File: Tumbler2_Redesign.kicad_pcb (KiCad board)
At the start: 2 copper layers, 77 x 84 mm, 113 parts, among them J1 Conn_01x02, J2 Conn_01x05, J3 Conn_01x10, J4 Conn_01x10, J5 USB_C_Receptacle_USB2.0_16P, J6 USB_C_Receptacle_USB2.0_16P, J7 Conn_01x04, J8 Conn_01x06, J9 Conn_01x06, Q1 MMBT3904, Q3 MMBT3904, SW1 SW_Push, SW2 SW_Push, SW3 SW_Push, U1 CH340C, U11 TB6612FNG, U12 AMS1117-5.0, U2 LSM6DSV, U3 AP63203WU, U4 ESP32-S3-WROOM-1, U8 USBLC6-2SC6, U9 USBLC6-2SC6

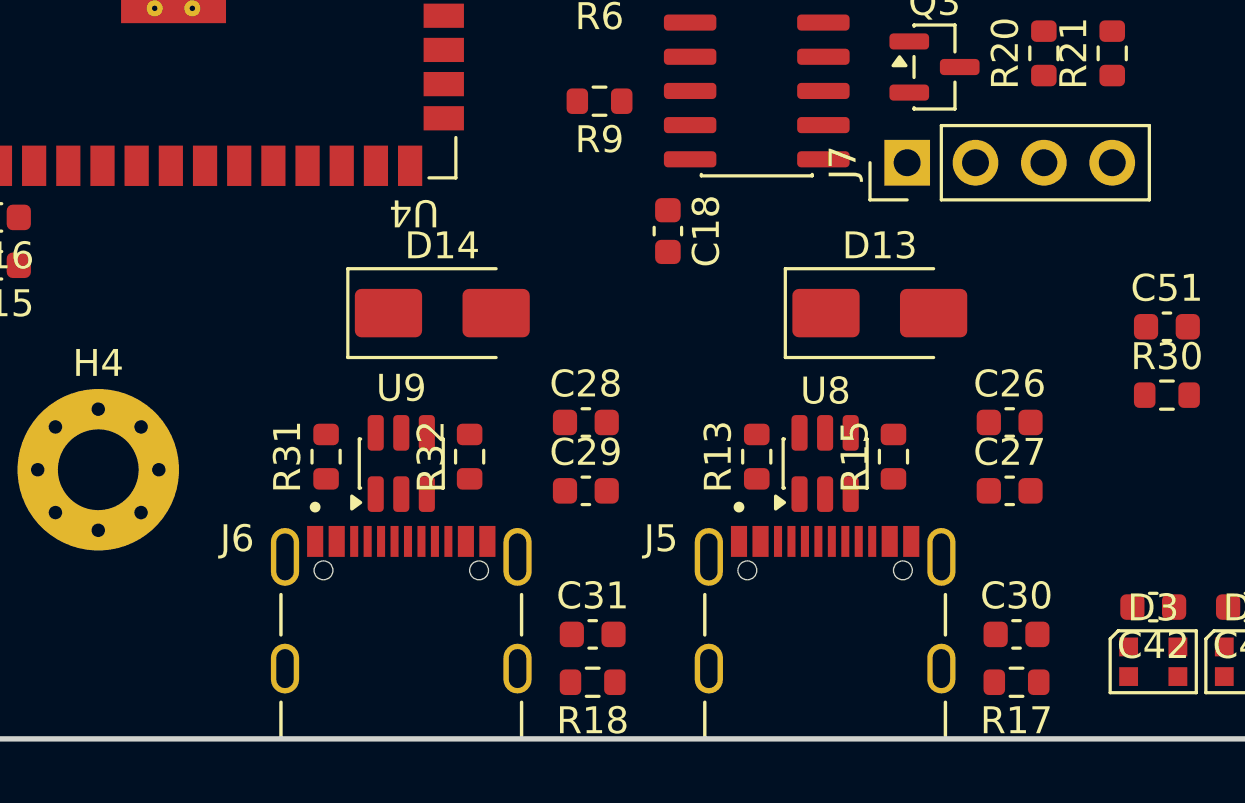
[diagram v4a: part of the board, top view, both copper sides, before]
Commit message: Fix bus merging and add net classes
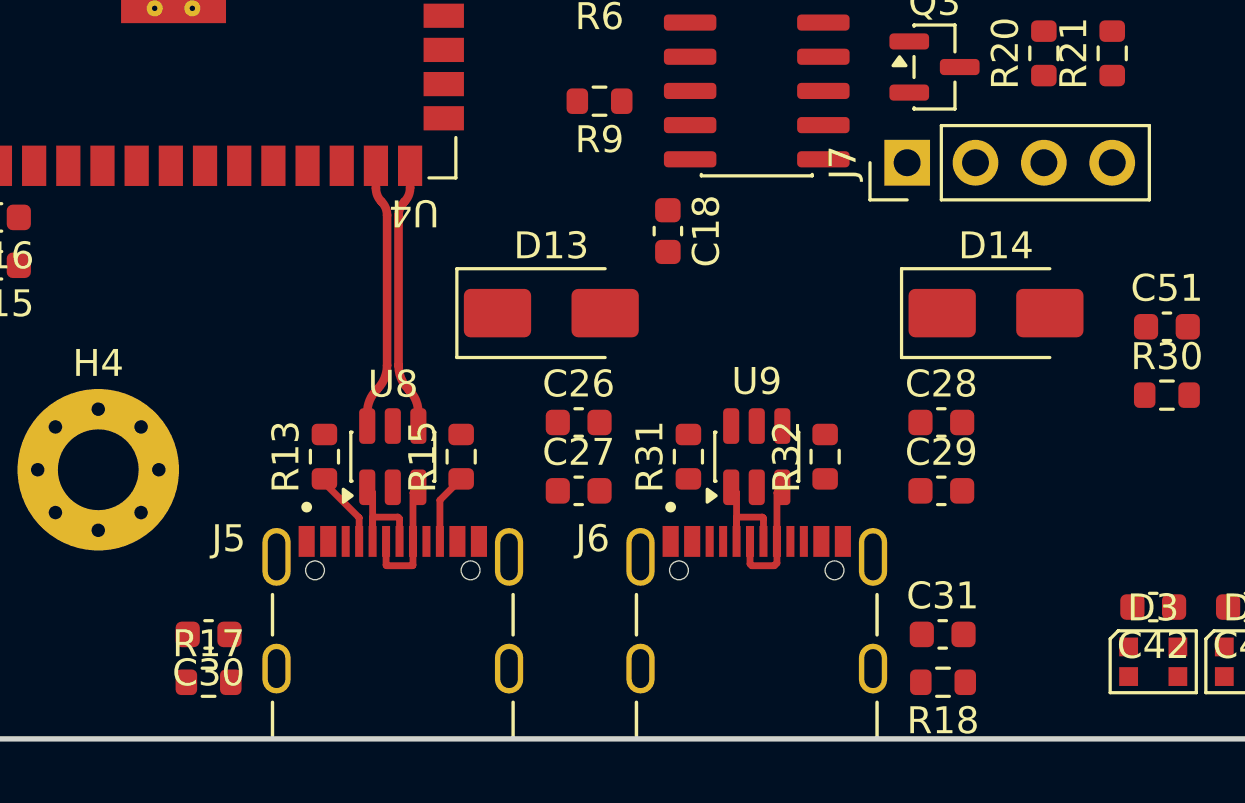
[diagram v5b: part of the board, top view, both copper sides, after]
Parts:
- moved C30 30.0 mm to (123.9, 141.5), turned to 180 degrees
- moved R17 30.0 mm to (123.9, 143.3), turned to 0 degrees
- moved D14 20.6 mm to (153.2, 129.5)
- moved U8 16.1 mm to (130.7, 134.9)
- moved J5 16.1 mm to (130.7, 142.7)
- moved R15 16.1 mm to (133.3, 134.9)
- moved R13 16.1 mm to (128.2, 134.9)
- moved C26 16.0 mm to (137.7, 133.6)
- moved C27 16.0 mm to (137.7, 136.1)
- moved R31 13.5 mm to (141.7, 134.9)
- moved U9 13.2 mm to (144.3, 134.9)
- moved C28 13.2 mm to (151.1, 133.6)
- moved C29 13.2 mm to (151.1, 136.1)
- moved J6 13.2 mm to (144.3, 142.7)
- moved R32 13.2 mm to (146.8, 134.9)
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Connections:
- J2 pad 1: /MCU/ENCA -> /MCU/ENCA_A
- J2 pad 2: /MCU/ENCB -> /MCU/ENCB_A
- J2 pad 3: /MCU/ENCA -> /MCU/ENCA_B
- J2 pad 4: /MCU/ENCB -> /MCU/ENCB_B
- R22 pad 2: /MCU/ENCB -> /MCU/ENCB_A
- R23 pad 2: /MCU/ENCA -> /MCU/ENCA_A
- R24 pad 2: /MCU/ENCB -> /MCU/ENCB_A
- R25 pad 2: /MCU/ENCA -> /MCU/ENCA_A
- R26 pad 2: /MCU/ENCB -> /MCU/ENCB_B
- R27 pad 2: /MCU/ENCA -> /MCU/ENCA_B
- R28 pad 2: /MCU/ENCB -> /MCU/ENCB_B
- R29 pad 2: /MCU/ENCA -> /MCU/ENCA_B
- U1 pad 5: /MCU/DP -> /MCU/DP_2
- U1 pad 6: /MCU/DM -> /MCU/DN_2
- U11 pad 15: /MCU/PWM -> /MCU/PWMB
- U11 pad 16: /MCU/IN2 -> /MCU/BIN2
- U11 pad 17: /MCU/IN1 -> /MCU/BIN1
- U11 pad 21: /MCU/IN1 -> /MCU/AIN1
- U11 pad 22: /MCU/IN2 -> /MCU/AIN2
- U11 pad 23: /MCU/PWM -> /MCU/PWMA
- U4 pad 10: /MCU/IN2 -> /MCU/BIN2
- U4 pad 11: /MCU/PWM -> /MCU/PWMB
- U4 pad 13: /MCU/DM -> /MCU/DN_1
- U4 pad 14: /MCU/DP -> /MCU/DP_1
- U4 pad 24: /MCU/ENCA -> /MCU/ENCA_B
- U4 pad 25: /MCU/ENCB -> /MCU/ENCB_B
- U4 pad 31: /MCU/ENCA -> /MCU/ENCA_A
- U4 pad 32: /MCU/IN1 -> /MCU/AIN1
- U4 pad 33: /MCU/IN2 -> /MCU/AIN2
- U4 pad 34: /MCU/PWM -> /MCU/PWMA
- U4 pad 35: /MCU/ENCB -> /MCU/ENCB_A
- U4 pad 9: /MCU/IN1 -> /MCU/BIN1
- U8 pad 4: /MCU/DP -> /MCU/DP_1
- U8 pad 6: /MCU/DM -> /MCU/DN_1
- U9 pad 4: /MCU/DP -> /MCU/DP_2
- U9 pad 6: /MCU/DM -> /MCU/DN_2
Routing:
- net /MCU/DP_1: track 0.00 -> 9.97 mm
- net /MCU/DN_1: track 0.00 -> 9.96 mm
- net Net-(J5-D+-PadA6): track 0.00 -> 4.87 mm
- net Net-(J6-D--PadA7): track 0.00 -> 4.86 mm
- net Net-(J5-D--PadA7): track 0.00 -> 4.85 mm
- net Net-(J6-D+-PadA6): track 0.00 -> 4.80 mm
- net Net-(J5-CC1): track 0.00 -> 2.86 mm
- net Net-(J5-CC2): track 0.00 -> 2.65 mm

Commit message: Start conceptual layouting
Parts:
- removed TP5, TP6, TP7: TestPoint, TestPoint:TestPoint_Pad_D1.5mm
- TP1, TP10, TP11, TP12, TP2, TP4: footprint TestPoint:TestPoint_Pad_D1.5mm -> TestPoint:TestPoint_THTPad_D1.0mm_Drill0.5mm
- moved R7 72.7 mm to (207.5, 106.9)
- moved R8 72.7 mm to (207.5, 103.4)
- moved TP11 51.1 mm to (207.8, 117.3)
- moved TP12 51.1 mm to (205.2, 117.3)
- moved R20 50.8 mm to (205.7, 122.1)
- moved R21 50.8 mm to (208.3, 122.1)
- moved R12 40.7 mm to (116.1, 130.6), turned to 0 degrees
- moved R11 40.0 mm to (116.1, 128.8), turned to 0 degrees
- moved C21 35.9 mm to (119.6, 127.0), turned to 0 degrees
- moved SW3 32.5 mm to (124.5, 130.8), turned to 180 degrees
- moved SW2 27.9 mm to (124.5, 125.7), turned to 180 degrees
- moved C41 26.7 mm to (139.4, 86.9), turned to 180 degrees
- moved R1 22.4 mm to (158.4, 105.4), turned to 0 degrees
- moved C32 20.5 mm to (167.6, 114.3), turned to -90 degrees
- moved TP4 19.9 mm to (145.0, 108.7)
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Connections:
- net /Peripherals/M1_M renamed /Peripherals/M1_N
- net /Peripherals/M2_M renamed /Peripherals/M2_N
- U4 pad 12: /MCU/IO8 -> /MCU/RGB
- U4 pad 23: /MCU/RGB -> /MCU/IO8
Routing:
- net /MCU/TXD: track 0.00 -> 42.9 mm
- net /MCU/RXD: track 0.00 -> 42.2 mm, vias 0 -> 2
- net /MCU/RGB: track 0.00 -> 39.4 mm, vias 0 -> 2
- net /MCU/RTS: track 0.00 -> 21.9 mm
- net /MCU/DTR: track 0.00 -> 18.5 mm, vias 0 -> 2
- net /MCU/BTN: track 0.00 -> 15.8 mm
- net /MCU/DP_2: track 0.00 -> 13.7 mm, vias 0 -> 2
- net /MCU/DN_2: track 0.00 -> 13.7 mm, vias 0 -> 2
- net /MCU/ENABLE: track 0.00 -> 12.0 mm
- net 3.3V: track 0.00 -> 9.83 mm
- net /MCU/GPIO0: track 0.00 -> 5.59 mm
- net Net-(J8-Pin_4): track 0.00 -> 3.81 mm
- net Net-(J8-Pin_3): track 0.00 -> 3.81 mm
- net Net-(J9-Pin_4): track 0.00 -> 3.80 mm
- net Net-(J9-Pin_3): track 0.00 -> 3.80 mm
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- added copper zone on F.Cu, net 3.3V
- added copper zone on B.Cu, net GND
- added copper zone on F.Cu, net GND
- added copper zone on F.Cu, net Net-(D11-A)
- added copper zone on F.Cu, net Net-(J1-Pin_2)
- added copper zone on F.Cu, net Net-(J5-SHIELD)
- added copper zone on F.Cu, net Net-(J6-SHIELD)
- added copper zone on F.Cu, net VBAT

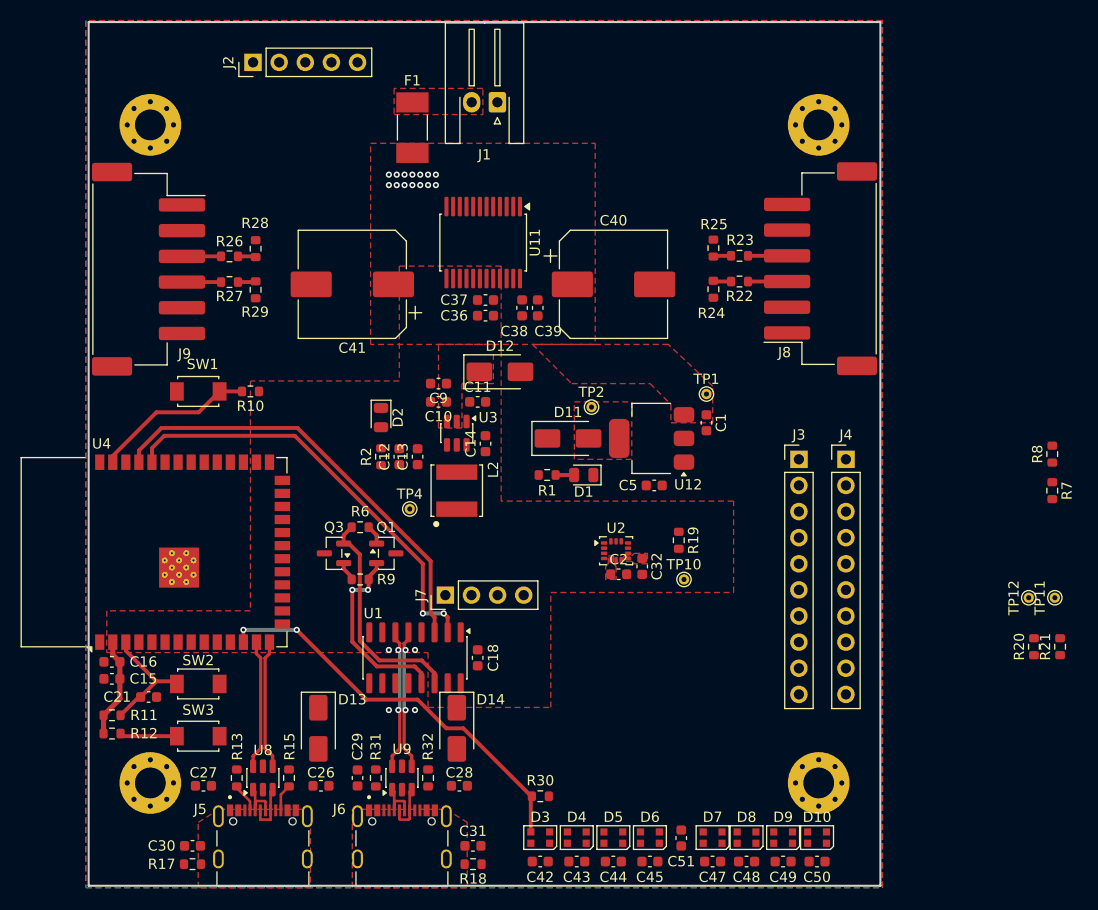
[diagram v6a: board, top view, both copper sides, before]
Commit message: Continue layout and update schematic
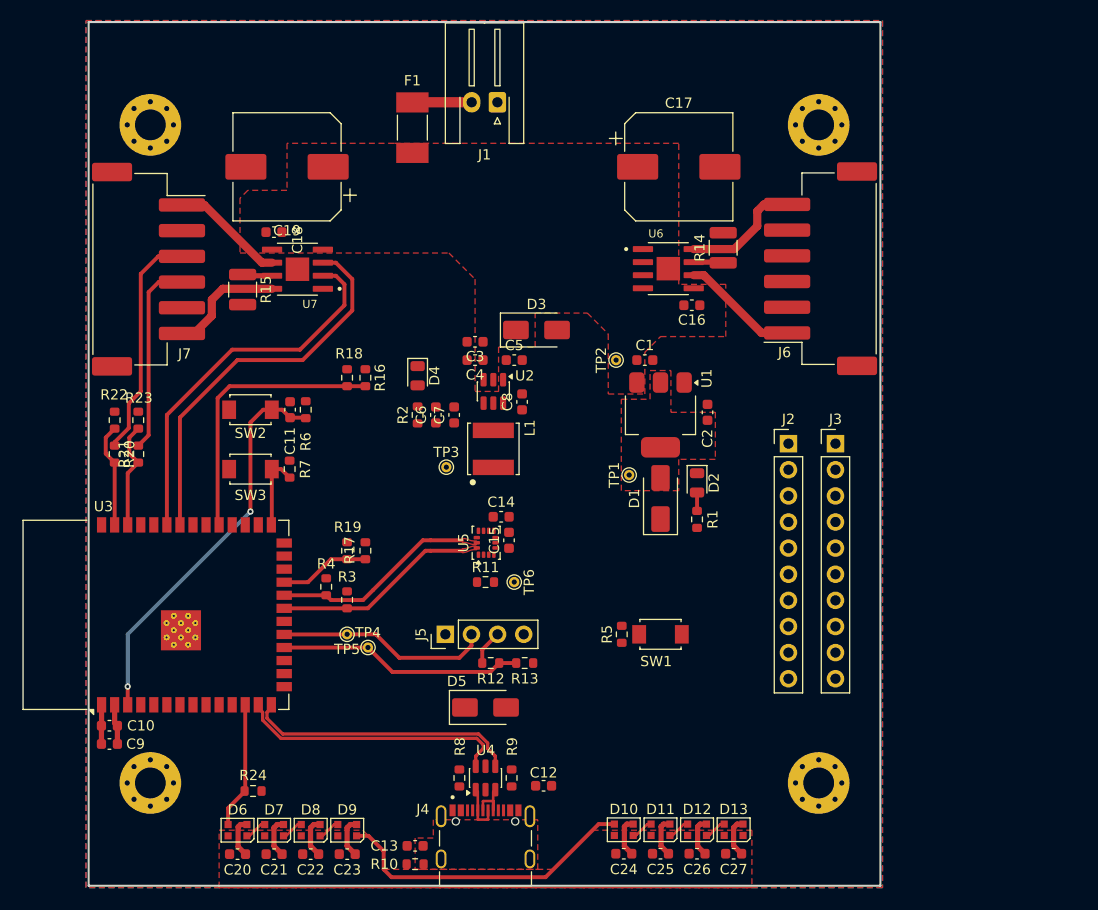
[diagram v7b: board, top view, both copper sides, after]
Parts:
- removed the C18 at (151.6, 123.2)
- removed the C27 at (125.0, 135.6)
- removed C28, C31, C37: 100nF, Capacitor_SMD:C_0603_1608Metric
- removed C29, C36, C39, C51: 10uF, Capacitor_SMD:C_0603_1608Metric
- removed D14: SS14, Diode_SMD:D_SMA
- removed the J2 at (129.8, 65.3)
- removed the J6 at (144.3, 142.7)
- removed Q1, Q3: MMBT3904, Package_TO_SOT_SMD:SOT-23
- removed the R18 at (151.2, 143.3)
- removed R31, R32: 5k1, Resistor_SMD:R_0603_1608Metric
- removed the R6 at (140.2, 110.5)
- removed the R9 at (140.2, 115.6)
- removed the U1 at (145.5, 123.2)
- removed U11: TB6612FNG, Package_SO:SSOP-24_5.3x8.2mm_P0.65mm
- removed U9: USBLC6-2SC6, Package_TO_SOT_SMD:SOT-23-6
- added C16: 100nF, Capacitor_SMD:C_0603_1608Metric, F.Cu at (172.5, 88.9)
- added R14: 220m, Resistor_SMD:R_1210_3225Metric, F.Cu at (175.5, 83.3)
- added R15: 220m, Resistor_SMD:R_1210_3225Metric, F.Cu at (128.8, 87.4)
- added U6: TB67H450FNG_EL, Tumbler2:SOIC127P599X175-9N, F.Cu at (170.2, 85.3)
- added U7: TB67H450FNG_EL, Tumbler2:SOIC127P599X175-9N, F.Cu at (134.1, 85.4)
- moved R4 71.8 mm to (136.9, 116.3)
- moved R3 69.4 mm to (138.9, 117.6), turned to 90 degrees
- moved TP4 67.0 mm to (141.0, 122.2), turned to 0 degrees
- moved TP5 66.4 mm to (138.9, 120.9), turned to 180 degrees
- moved R12 52.9 mm to (152.9, 123.7), turned to 0 degrees
- moved R13 52.1 mm to (156.2, 123.7), turned to 180 degrees
- moved SW1 50.8 mm to (169.4, 120.9), turned to 180 degrees
- moved R17 46.3 mm to (140.7, 112.8), turned to -90 degrees
- moved R19 46.2 mm to (138.9, 112.8)
- moved R5 43.2 mm to (165.7, 120.9), turned to 90 degrees
- moved R16 37.6 mm to (140.7, 95.9), turned to -90 degrees
- moved R18 36.7 mm to (138.9, 95.9), turned to -90 degrees
- moved R6 35.2 mm to (134.9, 99.1), turned to -90 degrees
- moved C17 33.7 mm to (171.2, 75.4), turned to 0 degrees
- moved C19 33.7 mm to (133.1, 75.4), turned to 180 degrees
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- renumbered C16 to C10, C21 to C11, C26 to C12, C30 to C13, C32 to C14, C2 to C15, C41 to C17, C38 to C18, C40 to C19, C5 to C2, C42 to C20, C43 to C21, C44 to C22, C45 to C23, C47 to C24, C48 to C25, C49 to C26, C50 to C27, C9 to C3, C10 to C4, C11 to C5, C12 to C6, C13 to C7, C14 to C8, C15 to C9, D11 to D1, D7 to D10, D8 to D11, D9 to D12, D10 to D13, D1 to D2, D12 to D3, D2 to D4, D13 to D5, D3 to D6, D4 to D7, D5 to D8, D6 to D9, J3 to J2, J4 to J3, J5 to J4, J7 to J5, J8 to J6, J9 to J7, L2 to L1, R17 to R10, R19 to R11, R20 to R12, R21 to R13, R22 to R16, R23 to R17, R24 to R18, R25 to R19, R26 to R20, R27 to R21, R28 to R22, R29 to R23, R30 to R24, R7 to R3, R8 to R4, R10 to R5, R11 to R6, R12 to R7, R13 to R8, R15 to R9, TP2 to TP1, TP1 to TP2, TP4 to TP3, TP11 to TP4, TP12 to TP5, TP10 to TP6, U12 to U1, U3 to U2, U4 to U3, U8 to U4, U2 to U5
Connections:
- net /MCU/DN_1 renamed /MCU/DN
- net /MCU/DP_1 renamed /MCU/DP
- U3 pad 10: /MCU/BIN2 -> unconnected-(U3-IO17-Pad10)
- U3 pad 11: /MCU/PWMB -> unconnected-(U3-IO18-Pad11)
- U3 pad 17: /MCU/IO9 -> /MCU/BTN
- U3 pad 18: /MCU/IO10 -> /MCU/ECHO
- U3 pad 19: /MCU/IO11 -> /MCU/TRIG
- U3 pad 23: /MCU/IO8 -> /MCU/ENCA_A
- U3 pad 24: /MCU/ENCA_B -> /MCU/AIN1
- U3 pad 25: /MCU/ENCB_B -> /MCU/AIN2
- U3 pad 31: /MCU/ENCA_A -> /MCU/ENCB_A
- U3 pad 32: /MCU/AIN1 -> unconnected-(U3-IO39-Pad32)
- U3 pad 33: /MCU/AIN2 -> unconnected-(U3-IO40-Pad33)
- U3 pad 34: /MCU/PWMA -> /MCU/BIN1
- U3 pad 35: /MCU/ENCB_A -> /MCU/BIN2
- U3 pad 36: /MCU/RXD -> unconnected-(U3-RXD0-Pad36)
- U3 pad 37: /MCU/TXD -> unconnected-(U3-TXD0-Pad37)
- U3 pad 38: /MCU/INT1 -> /MCU/ENCA_B
- U3 pad 39: /MCU/BTN -> /MCU/ENCB_B
- U3 pad 4: /MCU/ECHO -> /MCU/IO9
- U3 pad 5: /MCU/TRIG -> /MCU/INT1
- U3 pad 6: /MCU/IO6 -> /MCU/IO10
- U3 pad 7: /MCU/IO7 -> /MCU/IO11
- U3 pad 8: /MCU/STBY -> unconnected-(U3-IO15-Pad8)
- U3 pad 9: /MCU/BIN1 -> unconnected-(U3-IO16-Pad9)
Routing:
- net /MCU/TXD: track 42.9 -> 0.00 mm
- net /MCU/RXD: track 42.2 -> 0.00 mm, vias 2 -> 0
- net /MCU/BIN1: track 0.00 -> 38.1 mm
- net /MCU/BIN2: track 0.00 -> 36.9 mm
- net GND: track 0.00 -> 35.2 mm, vias 4 -> 0
- net Net-(D10-DIN): track 0.00 -> 29.9 mm
- net /MCU/RGB: track 39.4 -> 12.3 mm, vias 2 -> 0
- net /MCU/ENABLE: track 12.0 -> 38.6 mm, vias 0 -> 2
- net /MCU/ENCB_A: track 1.75 -> 27.2 mm
- net /MCU/ECHO: track 0.00 -> 23.9 mm
- net /MCU/RTS: track 21.9 -> 0.00 mm
- net /MCU/TRIG: track 0.00 -> 20.8 mm
- net /MCU/SCL: track 0.00 -> 19.9 mm
- net /MCU/SDA: track 0.00 -> 19.6 mm
- net Net-(J7-Pin_3): track 3.80 -> 22.5 mm
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- added copper zone on F.Cu, net /MCU/SCL
- added copper zone on F.Cu, net /MCU/SDA
- added copper zone on F.Cu, net 5V
- removed copper zone on F.Cu, net 3.3V
- removed copper zone on F.Cu, net Net-(J1-Pin_2)
- removed copper zone on F.Cu, net Net-(J6-SHIELD)
